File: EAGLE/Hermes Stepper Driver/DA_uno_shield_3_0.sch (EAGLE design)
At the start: 16 parts

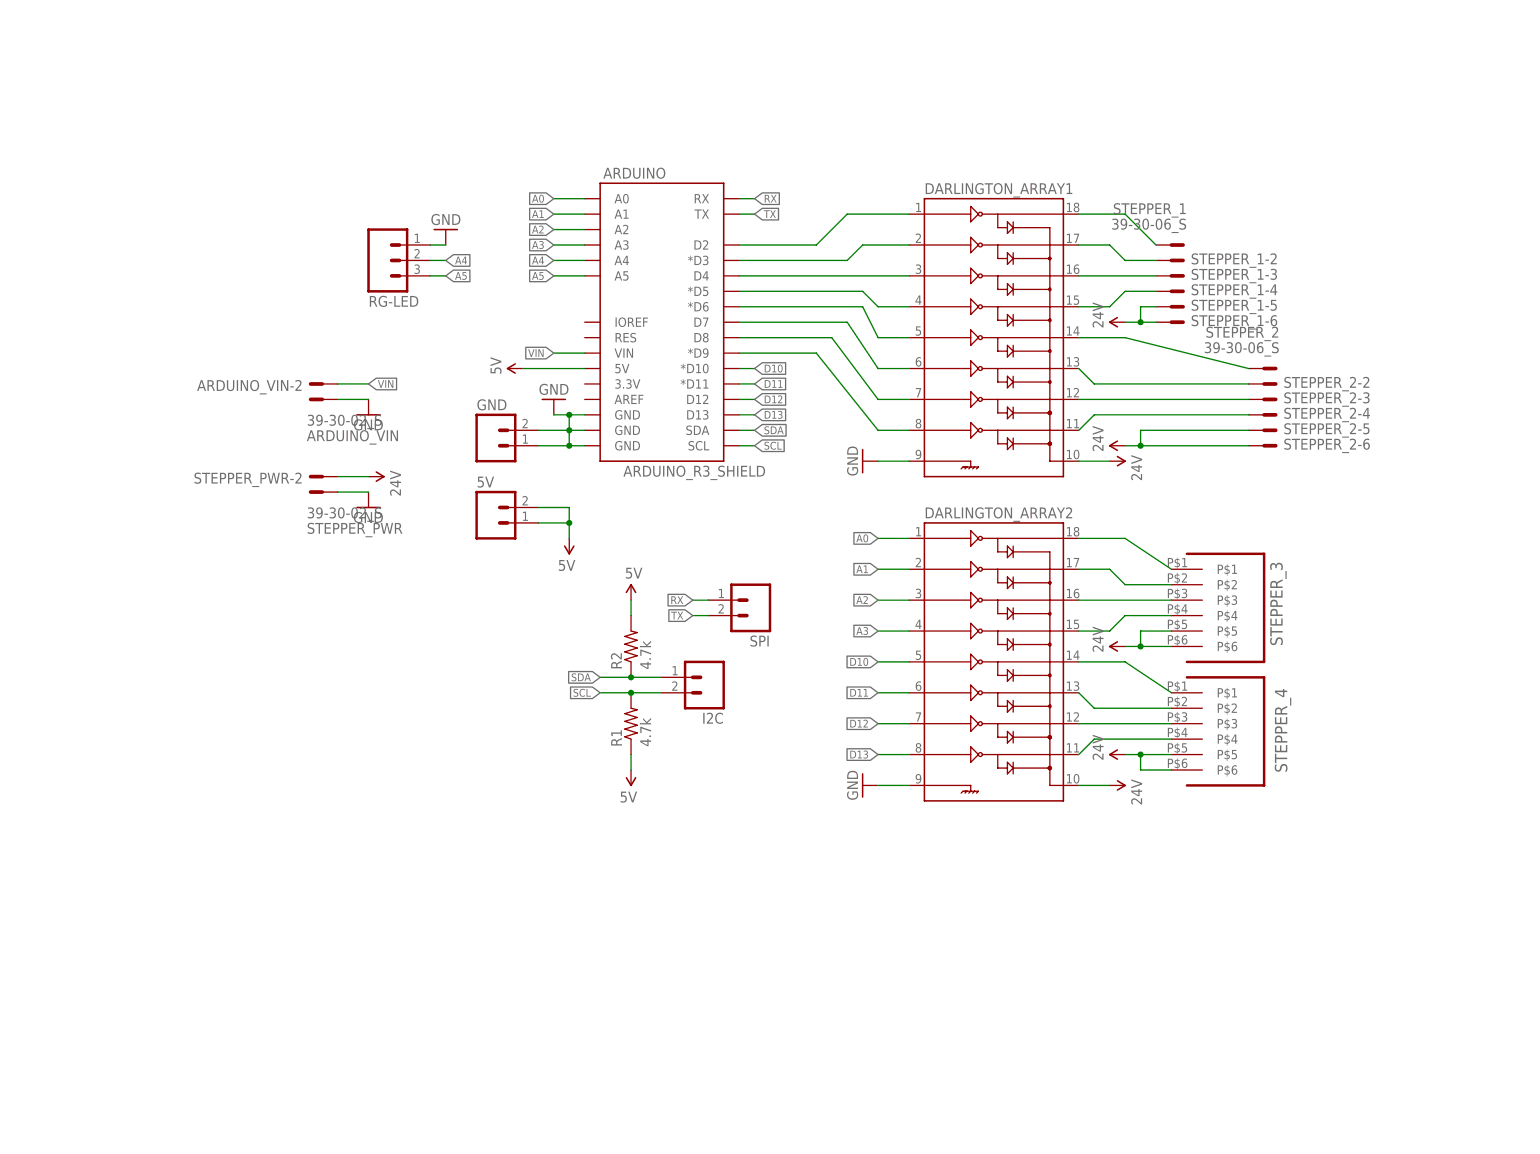
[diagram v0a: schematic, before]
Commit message: got rid of some things that should not have been there, updated the firmware
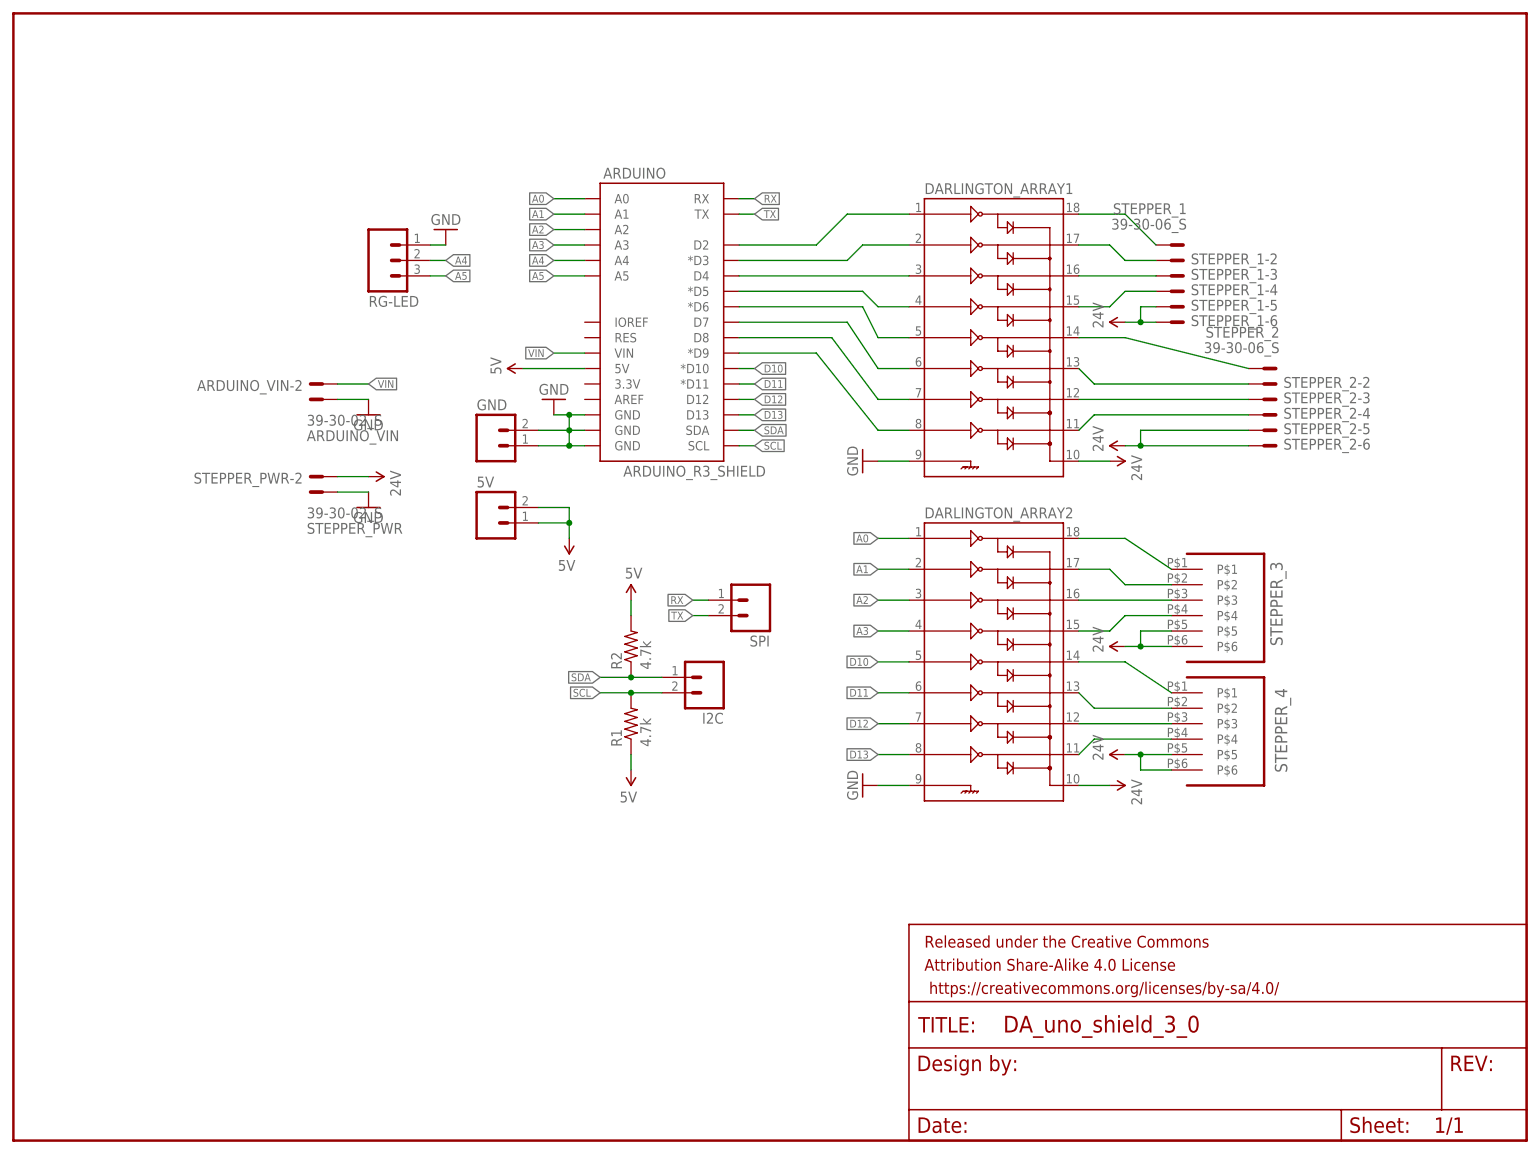
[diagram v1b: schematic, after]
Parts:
- added FRAME1: FRAME-LETTER, SparkFun-Aesthetics:FRAME-LETTER
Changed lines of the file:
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@@
 <?xml version="1.0" encoding="utf-8"?>
 <!DOCTYPE eagle SYSTEM "eagle.dtd">
-<eagle version="7.5.0">
+<eagle version="7.7.0">
 <drawing>
 <settings>
@@
 <layers>
 <layer number="1" name="Top" color="4" fill="1" visible="no" active="no"/>
+<layer number="2" name="Route2" color="1" fill="3" visible="no" active="no"/>
+<layer number="3" name="Route3" color="4" fill="3" visible="no" active="no"/>
+<layer number="14" name="Route14" color="1" fill="6" visible="no" active="no"/>
+<layer number="15" name="Route15" color="4" fill="6" visible="no" active="no"/>
 <layer number="16" name="Bottom" color="1" fill="1" visible="no" active="no"/>
 <layer number="17" name="Pads" color="2" fill="1" visible="no" active="no"/>
@@
 <part name="STEPPER_3" library="MTIID-molex-mini-fit-with-some-vertical" deviceset="39-29-?06?" device=""/>
 <part name="STEPPER_4" library="MTIID-molex-mini-fit-with-some-vertical" deviceset="39-29-?06?" device=""/>
+<part name="FRAME1" library="SparkFun-Aesthetics" deviceset="FRAME-LETTER" device=""/>
 </parts>
 <sheets>
@@
 <attribute name="NAME" x="153.67" y="-22.098" size="2.032" layer="95" rot="MR270"/>
 </instance>
+<instance part="FRAME1" gate="G$1" x="-55.88" y="-96.52"/>
+<instance part="FRAME1" gate="V" x="91.44" y="-96.52"/>
 </instances>
 <busses>
